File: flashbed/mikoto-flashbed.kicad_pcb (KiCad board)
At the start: 2 copper layers, 54 x 41.5 mm, 65 parts, among them J1 Conn_01x01, J2 Conn_01x01, J3 Conn_01x01, J4 Conn_01x01, J7 Conn_01x05, SW1 TVBP06, U1 mikoto-pins

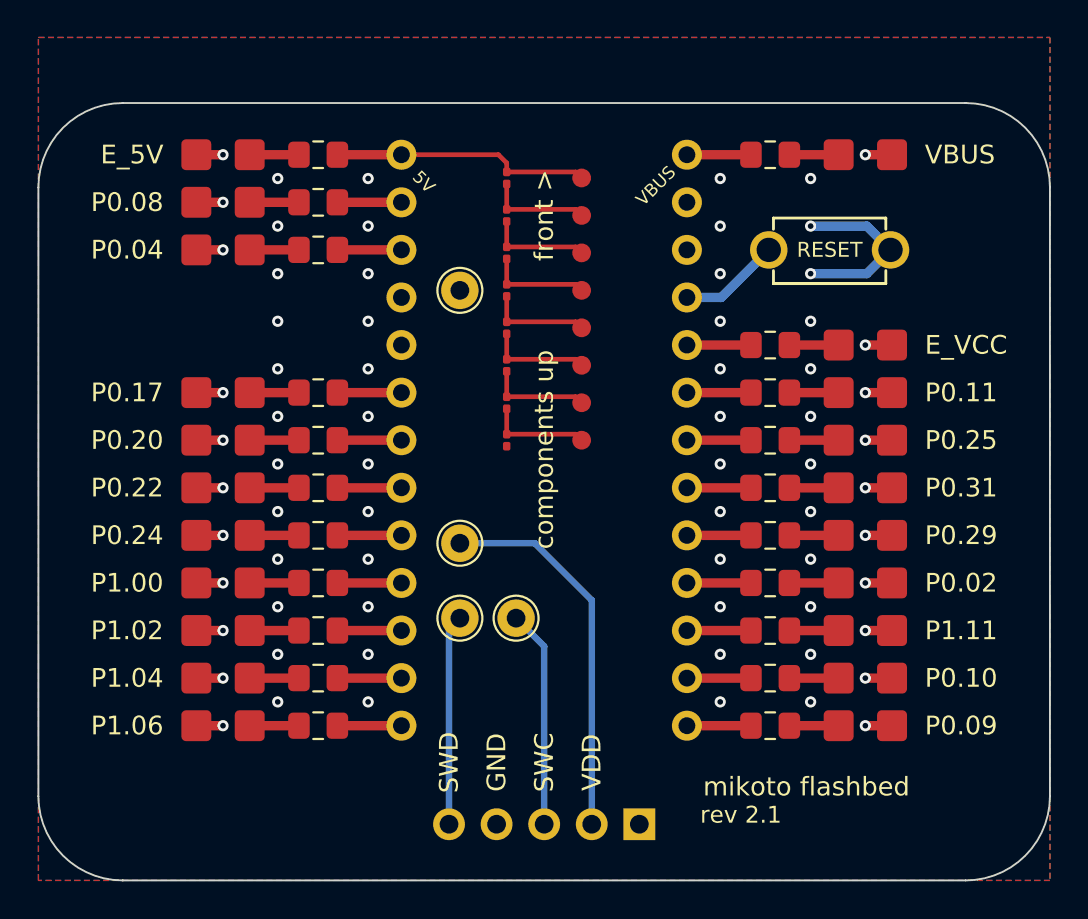
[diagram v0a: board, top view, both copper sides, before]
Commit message: update flashbed for new underside pad placement
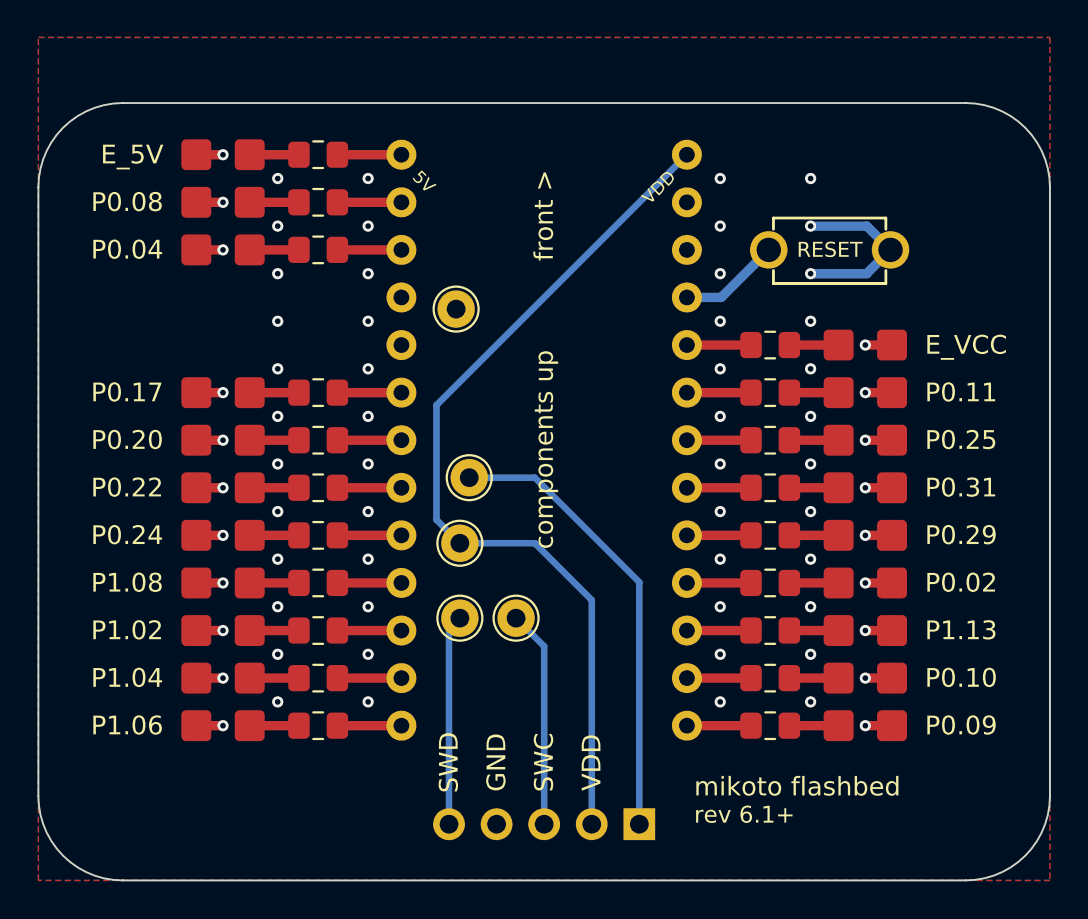
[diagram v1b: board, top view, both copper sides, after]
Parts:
- removed D21: LED_Small, footprints:LED_1206_3216M_Castellated-nosilk
- removed R21: 2.2k, Resistor_SMD:R_0805_2012Metric_Pad1.15x1.40mm_HandSolder
- removed R22, R23, R24, R25, R26, R27, R28, R29: R_Small, Resistor_SMD:R_0201_0603Metric
- removed TP1, TP2, TP3, TP4, TP5, TP6, TP7, TP8: TestPoint, footprints:TestPoint_Pad_D1.0mm-nosilk
- added J5: Conn_01x01, TestPoint:TestPoint_THTPad_D2.0mm_Drill1.0mm, F.Cu at (-4.00, 2.00)
- U1: footprint footprints:mikoto-pins-bigger-holes -> footprints:mikoto-pins
- moved J2 1.02 mm to (-4.70, -7.00)
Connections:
- net P1.00 renamed P1.08
- net P1.11 renamed P1.13
- J7 pad 1: unconnected-(J7-Pad1) -> SWO
- U1 pad 26: VBUS -> VDD
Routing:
- net VDD: track 20.3 -> 47.1 mm
- net SWO: track 0.00 -> 24.3 mm
- net EXT_5V: track 13.8 -> 3.42 mm
- net Net-(R27-Pad1): track 5.49 -> 0.00 mm
- net Net-(R28-Pad1): track 5.49 -> 0.00 mm
- net Net-(R26-Pad1): track 5.49 -> 0.00 mm
- net Net-(R25-Pad1): track 5.49 -> 0.00 mm
- net Net-(R24-Pad1): track 5.49 -> 0.00 mm
- net Net-(R23-Pad1): track 5.49 -> 0.00 mm
- net Net-(R22-Pad1): track 5.49 -> 0.00 mm
- net VBUS: track 3.42 -> 0.00 mm
- net Net-(D21-Pad2): track 2.57 -> 0.00 mm
- net GND: track 40.8 -> 39.3 mm, vias 69 -> 68
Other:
- board text added: "P1.08"
- board text added: "P1.13"
- board text added: "rev 6.1+"
- board text removed: "P1.00"
- board text removed: "P1.11"
- board text removed: "VBUS"
- board text removed: "rev 2.1"

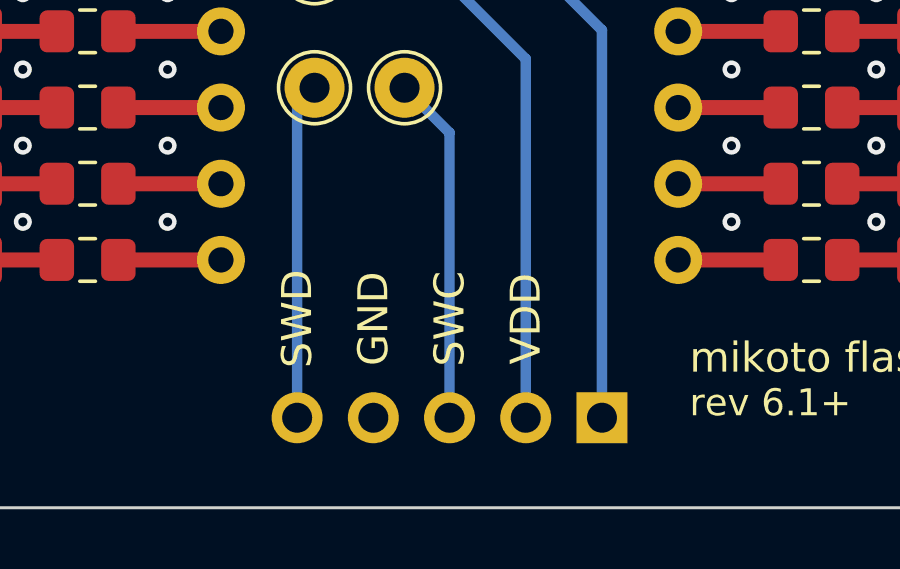
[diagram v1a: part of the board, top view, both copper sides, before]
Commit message: add swo label to flashbed
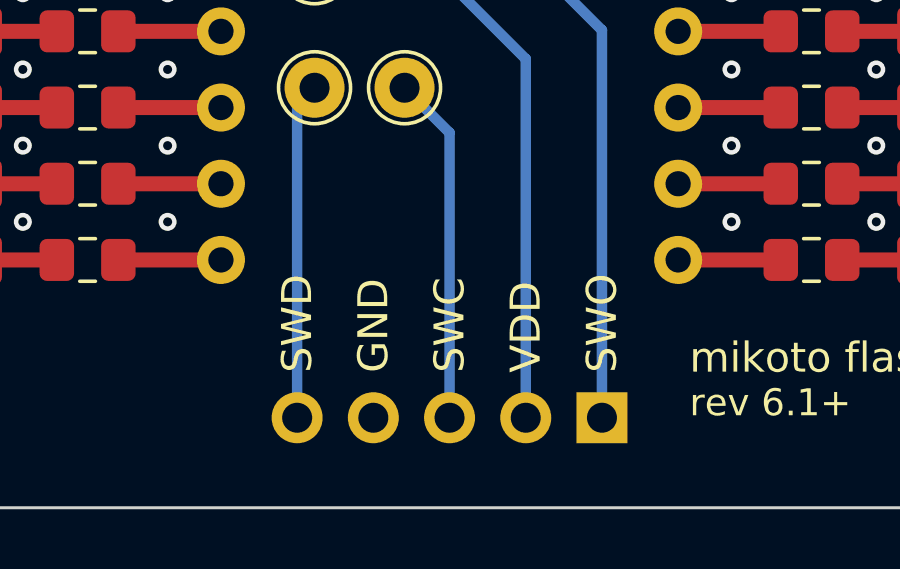
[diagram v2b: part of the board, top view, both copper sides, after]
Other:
- board text added: "SWO"
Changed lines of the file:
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@@
       (usegerberattributes true)
       (usegerberadvancedattributes true)
-      (creategerberjobfile true)
+      (creategerberjobfile false)
       (svguseinch false)
       (svgprecision 6)
@@
       (psnegative false)
       (psa4output false)
-      (plotreference true)
-      (plotvalue true)
+      (plotreference false)
+      (plotvalue false)
       (plotinvisibletext false)
       (sketchpadsonfab false)
@@
     (effects (font (size 1 1) (thickness 0.15)) (justify left))
   )
-  (gr_text "SWD" (at -5.08 17.2 90) (layer "F.SilkS")
-    (effects (font (size 1 1) (thickness 0.15)))
+  (gr_text "SWD" (at -5.08 19 90) (layer "F.SilkS")
+    (effects (font (size 1 1) (thickness 0.15)) (justify left))
   )
   (gr_text "P1.02" (at -20.32 10.16) (layer "F.SilkS")
     (effects (font (size 1 1) (thickness 0.15)) (justify right))
   )
+  (gr_text "SWO" (at 5.08 19 90) (layer "F.SilkS")
+    (effects (font (size 1 1) (thickness 0.15)) (justify left))
+  )
   (gr_text "P0.09" (at 20.32 15.24) (layer "F.SilkS")
     (effects (font (size 1 1) (thickness 0.15)) (justify left))
@@
     (effects (font (size 1 1) (thickness 0.15)) (justify right))
   )
-  (gr_text "VDD" (at 2.54 17.2 90) (layer "F.SilkS")
-    (effects (font (size 1 1) (thickness 0.15)))
+  (gr_text "VDD" (at 2.54 19 90) (layer "F.SilkS")
+    (effects (font (size 1 1) (thickness 0.15)) (justify left))
   )
   (gr_text "P0.02" (at 20.32 7.62) (layer "F.SilkS")
@@
     (effects (font (size 1 1) (thickness 0.15)) (justify right))
   )
-  (gr_text "GND" (at -2.54 17.2 90) (layer "F.SilkS")
-    (effects (font (size 1 1) (thickness 0.15)))
+  (gr_text "GND" (at -2.54 19 90) (layer "F.SilkS")
+    (effects (font (size 1 1) (thickness 0.15)) (justify left))
   )
   (gr_text "P0.04" (at -20.32 -10.16) (layer "F.SilkS")
@@
     (effects (font (size 1 1) (thickness 0.15)) (justify left))
   )
-  (gr_text "SWC" (at 0 17.2 90) (layer "F.SilkS")
-    (effects (font (size 1 1) (thickness 0.15)))
+  (gr_text "SWC" (at 0 19 90) (layer "F.SilkS")
+    (effects (font (size 1 1) (thickness 0.15)) (justify left))
   )
   (gr_text "P0.22" (at -20.32 2.54) (layer "F.SilkS")
